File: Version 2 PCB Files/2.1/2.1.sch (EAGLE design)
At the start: 54 parts, among them IC1 FT230XS, IC4 L4931D, X1 MINI-USB-32005-301

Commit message: saving to git
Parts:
- removed C11: .1uf, rcl:C-EUC0603K
- removed C12, C13, C17, C18: 1uF, rcl:C-EUC0603K
- removed C14, C15: 2.2uF, rcl:C-EUC0603K
- removed C16: .1uF, rcl:C-EUC0603K
- removed JP1: (no value), adafruit:PINHD-1X6B
- removed JP4, JP5: (no value), adafruit:PINHD-1X1
- removed LED1, LED2, LED3: (no value), adafruit:LEDSMT1206
- removed R12: 2K, eagle-ltspice:RR0603
- removed R14: 390K, eagle-ltspice:RR0603
- removed R17, R18, R19: 330, eagle-ltspice:RR0603
- removed U$4: ATMEGA32U4-AU, adafruit:ATMEGA32U4-AU
- added IC2: ATMEGA644A, atmel:ATMEGA644A
- added J1: XF2L-1025-1A, 10pinzif:XF2L-1025-1A
- added JP2: (no value), adafruit:PINHD-1X6B
- added JP6, JP7: (no value), adafruit:PINHD-1X1
- added LED5, LED6, LED7: (no value), adafruit:LEDSMT1206
- added R10, R11, R15: 330, eagle-ltspice:RR0603
- R13: value 2K -> 100
- U$3: value UG-2864HSWEG01 -> AT45DB641E; device adafruit:UG-2864HSWEG01 -> MyParts:AT45DB641E
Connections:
- removed net N$10: C13.1, U$3.C2N
- removed net N$14: C18.2, U$4.UCAP
- removed net N$17: LED1.A, R17.1
- removed net N$18: LED2.A, R18.1
- removed net N$19: LED3.A, R19.1
- removed net N$21: R19.2, U$4.PB5(OC1A/ADC12/!OC4B)
- removed net N$22: R18.2, U$4.PB6(OC1B/OC4B/ADC13)
- removed net N$7: C13.2, U$3.C2P
- removed net N$8: C17.1, U$3.C1P
- removed net N$9: R14.1, U$3.IREF
- removed net OLED_SCL: R12.1, U$3.D0/DI, U$4.PD0(INT0/OC0B/SCL)
- removed net OLED_SDA: R13.1, U$3.D1/SCLK, U$3.D2, U$4.PD1(INT1/SDA)
- new net ANODE: IC2.(PCINT31/OC2A)PD7, J1.1
- new net CS: IC2.(PCINT19/TMS)PC3
- new net KATHODE: J1.2, R13.1
- new net N$11: LED5.A, R10.1
- new net N$12: LED6.A, R11.1
- new net N$13: LED7.A, R15.1
- new net N$15: IC2.(PCINT28/OC1B)PD4, R15.2
- new net N$16: IC2.(PCINT29/OC1A)PD5, R11.2
- new net N$20: IC2.(PCINT30/OC2B/ICP)PD6, R10.2
- new net N$24: IC2.(PCINT25/TXD0)PD1, JP6.1
- new net N$26: J1.12
- new net N$27: J1.11
- new net N1: J1.7
- new net RST: IC2.(PCINT18/TCK)PC2
- new net RXD1: IC2.(PCINT24/RXD0)PD0, JP7.1
- new net SCL: J1.9
- new net SDA: J1.8
- net B0: now also IC2.(PCINT26/INT0)PD2; no longer U$4.PD4(ICP1/ADC8)
- net B1: now also IC2.(PCINT27/INT1)PD3; no longer U$4.PD5(XCK/CTS)
- net B2: now also IC2.(PCINT10/INT2/AIN0)PB2; no longer U$4.PD6(T1/ADC9/!OC4D)
- net GND: now also IC2.GND, IC2.GND@1, IC2.GND@2, IC2.GND@3, J1.3, J1.5, JP2.6, LED5.C, LED6.C, LED7.C, R13.2; no longer C11.1, C12.1, C14.1, C15.1, C16.1, C18.1, JP1.6, LED1.C, LED2.C, LED3.C, R14.2, U$3./CS, U$3.BS0, U$3.BS2, U$3.D/C, U$3.E/RD, U$3.MT, U$3.MT2, U$3.R/W, U$3.VLSS, U$3.VSS, U$4.GND, U$4.GND1, U$4.GND2, U$4.GND3, U$4.UGND
- net MISO: now also IC2.(PCINT14/MISO)PB6, JP2.3; no longer JP1.3, U$4.PB3(PDO/MISO)
- net MOSI: now also IC2.(PCINT13/MOSI)PB5, JP2.4; no longer JP1.4, U$4.PB2(PDI/MOSI)
- net N$23: now also J1.6; no longer R17.2, U$4.PB7(OC0A/OC1C/RTS)
- net N$5: now also IC2.(PCINT16/SCL)PC0; no longer C14.2, U$3.VCOMH
- net N$6: now also IC2.(PCINT17/SDA)PC1; no longer C17.2, U$3.C1N
- net RESET: now also IC2.RESET, JP2.2; no longer JP1.2, U$4./RESET
- net RXD: no longer JP5.1, U$4.PD2(INT2/RXD1)
- net SCK: now also IC2.(PCINT15/SCK)PB7, JP2.5; no longer JP1.5, U$4.PB1(SCK)
- net TXD: no longer JP4.1, U$4.PD3(INT3/TXD1)
- net VCC: now also IC2.AVCC, IC2.VCC, IC2.VCC@1, IC2.VCC@2, J1.10, J1.4; no longer C11.2, C12.2, C15.2, C16.2, JP1.1, R12.2, R13.2, U$3./RES, U$3.BS1, U$3.VBAT, U$3.VCC, U$3.VDD, U$4.AVCC, U$4.AVCC1, U$4.VCC, U$4.VCC1
- net VDD: now also JP2.1
- net VUSB: no longer U$4.UVCC, U$4.VBUS
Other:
- moved on the sheet: LED4, R13

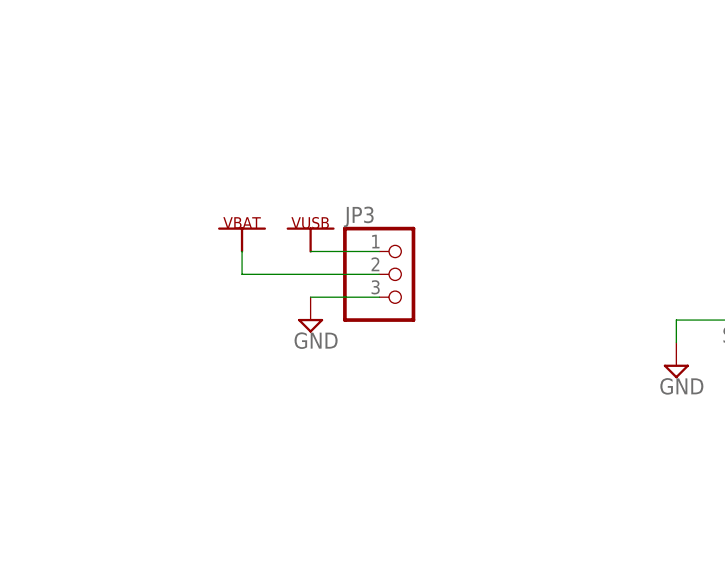
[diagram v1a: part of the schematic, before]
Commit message: Added a way to bypass LIPO charging circuitry which wont be ready for the next prototype
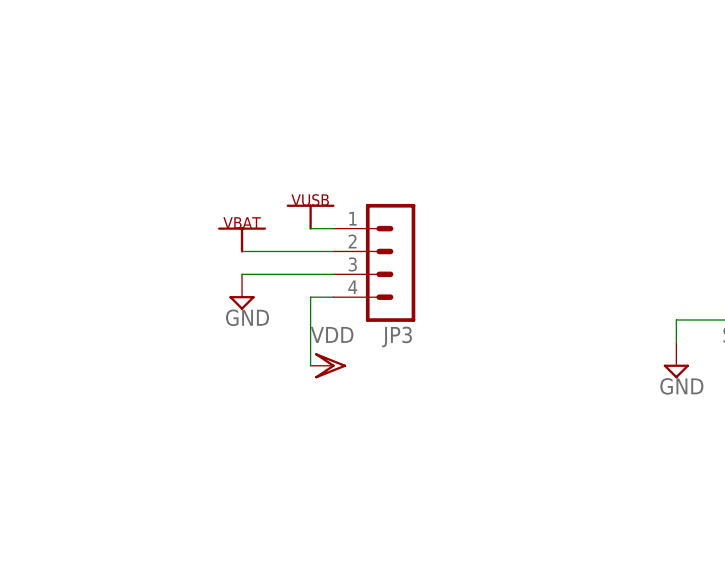
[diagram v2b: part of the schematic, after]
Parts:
- JP3: device adafruit:PINHD-1X3 -> con-lstb:MA04-1
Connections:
- net VDD: now also JP3.4
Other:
- note added: "EXTRA CONNETION FOR VDD"
- note added: "Extra Vdd connection to bypass all the lipo circuitry for the second prototype"
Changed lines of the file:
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@@
 <part name="SUPPLY8" library="supply2" deviceset="GND" device=""/>
 <part name="SUPPLY9" library="supply2" deviceset="GND" device=""/>
-<part name="JP3" library="adafruit" deviceset="PINHD-1X3" device=""/>
+<part name="JP3" library="con-lstb" deviceset="MA04-1" device=""/>
 <part name="P+4" library="supply1" deviceset="VCC" device=""/>
 <part name="LED4" library="adafruit" deviceset="LED" device="SMT1206"/>
@@
 <part name="R13" library="eagle-ltspice" deviceset="R" device="R0603" value="100"/>
 <part name="U$3" library="MyParts" deviceset="AT45DB641E" device=""/>
+<part name="VDD4" library="supply1" deviceset="VDD" device=""/>
 </parts>
 <sheets>
@@
 <wire x1="-40.64" y1="81.28" x2="-129.54" y2="81.28" width="1.27" layer="98"/>
 <wire x1="-129.54" y1="81.28" x2="-129.54" y2="-40.64" width="1.27" layer="98"/>
+<text x="-220.98" y="60.96" size="1.778" layer="255">EXTRA CONNETION FOR VDD</text>
+<text x="-220.98" y="50.8" size="1.778" layer="255">Extra Vdd connection
+to bypass all the lipo
+circuitry for the second prototype</text>
 </plain>
 <instances>
@@
 <instance part="SUPPLY8" gate="GND" x="22.86" y="111.76"/>
 <instance part="SUPPLY9" gate="GND" x="50.8" y="96.52"/>
-<instance part="JP3" gate="A" x="-198.12" y="38.1"/>
+<instance part="JP3" gate="1" x="-198.12" y="38.1" rot="R180"/>
 <instance part="P+4" gate="VCC" x="-111.76" y="17.78"/>
 <instance part="LED4" gate="G$1" x="-111.76" y="10.16" rot="R180"/>
@@
 <instance part="U$6" gate="G$1" x="-223.52" y="124.46"/>
 <instance part="U$7" gate="G$1" x="-215.9" y="40.64"/>
-<instance part="U$8" gate="G$1" x="-208.28" y="40.64"/>
-<instance part="SUPPLY20" gate="GND" x="-208.28" y="33.02"/>
+<instance part="U$8" gate="G$1" x="-208.28" y="43.18"/>
+<instance part="SUPPLY20" gate="GND" x="-215.9" y="35.56"/>
 <instance part="U$9" gate="G$1" x="-154.94" y="40.64"/>
 <instance part="SUPPLY21" gate="GND" x="-167.64" y="27.94"/>
@@
 <instance part="R13" gate="G$1" x="17.78" y="45.72" rot="MR0"/>
 <instance part="U$3" gate="G$1" x="-22.86" y="30.48"/>
+<instance part="VDD4" gate="G$1" x="-205.74" y="27.94" rot="R270"/>
 </instances>
 <busses>
@@
 </segment>
 <segment>
-<pinref part="JP3" gate="A" pin="3"/>
-<wire x1="-200.66" y1="35.56" x2="-208.28" y2="35.56" width="0.1524" layer="91"/>
+<pinref part="JP3" gate="1" pin="3"/>
+<wire x1="-205.74" y1="38.1" x2="-215.9" y2="38.1" width="0.1524" layer="91"/>
 <pinref part="SUPPLY20" gate="GND" pin="GND"/>
 </segment>
@@
 </segment>
 <segment>
-<pinref part="JP3" gate="A" pin="1"/>
-<wire x1="-208.28" y1="40.64" x2="-200.66" y2="40.64" width="0.1524" layer="91"/>
+<pinref part="JP3" gate="1" pin="1"/>
+<wire x1="-208.28" y1="43.18" x2="-205.74" y2="43.18" width="0.1524" layer="91"/>
 <pinref part="U$8" gate="G$1" pin="VUSB"/>
 </segment>
@@
 </segment>
 <segment>
-<pinref part="JP3" gate="A" pin="2"/>
+<pinref part="JP3" gate="1" pin="2"/>
 <pinref part="U$7" gate="G$1" pin="VBAT"/>
-<wire x1="-200.66" y1="38.1" x2="-215.9" y2="38.1" width="0.1524" layer="91"/>
-<wire x1="-215.9" y1="38.1" x2="-215.9" y2="40.64" width="0.1524" layer="91"/>
+<wire x1="-205.74" y1="40.64" x2="-215.9" y2="40.64" width="0.1524" layer="91"/>
 </segment>
 </net>
@@
 <pinref part="VDD3" gate="G$1" pin="VDD"/>
 </segment>
-</net>
+<segment>
+<pinref part="JP3" gate="1" pin="4"/>
+<wire x1="-205.74" y1="35.56" x2="-208.28" y2="35.56" width="0.1524" layer="91"/>
+<wire x1="-208.28" y1="35.56" x2="-208.28" y2="27.94" width="0.1524" layer="91"/>
+<pinref part="VDD4" gate="G$1" pin="VDD"/>
+</segment>
+</net>
